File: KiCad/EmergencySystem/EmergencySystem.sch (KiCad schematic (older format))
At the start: 26 parts, among them K1 HE1AN-S-DC12V, K2 HE1AN-S-DC12V, M1 Left_Motor, M2 Right_Motor, SW1 E-StopButton01, SW2 E-StopButton02, SW3 ON/OFF_Switch, SW4 ON/OFF_Switch, SW5 E-Stop_Switch, U1 T3_EmergencyLight_RED, U10 Adafruit_2200mAh_LiPo, U11 OLED_I2C_Display, U2 T3_EmergencyLight_BLUE, U3 T3_EmergencyLight_AMBER, U4 e-Boot_BuckConverter, U5 Elegoo_4RelayModule, U6 Feather_32u4_RFM95, U7 Adafruit_2200mAh_LiPo, U8 Feather_32u4_RFM95, U9 e-Boot_BuckConverter

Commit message: Updated KiCad Schematics
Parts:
- removed SW1: E-StopButton01, symbol Switch:SW_Push_Open
- removed SW2: E-StopButton02, symbol Switch:SW_Push_Open
- removed SW3: ON/OFF_Switch, symbol Switch:SW_SPST
- added SW1: E-Stop_Switch, symbol Switch:SW_SPST
- added SW3: E-StopButton02, symbol Switch:SW_Push_Open
- added SW4: E-StopButton01, symbol Switch:SW_Push_Open
- SW5: value E-Stop_Switch -> ON/OFF_Switch
- renumbered AE2 to AE1, AE1 to AE2, CB2 to CB1, CB1 to CB2, K2 to K1, K1 to K2, M2 to M1, M1 to M2, SW4 to SW2, U8 to U1, U7 to U10, U9 to U11, U1 to U2, U2 to U3, U3 to U4, U10 to U5, U11 to U6, U5 to U7, U4 to U8, U6 to U9
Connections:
- net GND: now also SW2.2 (B), SW1.2 (B), SW3.1 (A)
- net at U9.1 (TXD1/INT3): now also R2.2, SW4.1 (A)
- net at U9.12 (A11): no longer R1.2
- net at U1.1 (TXD1/INT3): now also R1.2, SW1.1 (A)
- new net: SW5.1 (A), U9.~ (EXT_ANT)
- new net: U10.~ (V-), U9.~ (EXT_ANT)
- new net: U1.~ (EXT_ANT), U5.~ (V-)
- new net: SW3.2 (B), SW4.2 (B)
- now unconnected: U1.12 (A11)
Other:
- moved on the sheet: AE1, AE2, SW2, U1, U11, U5, U6

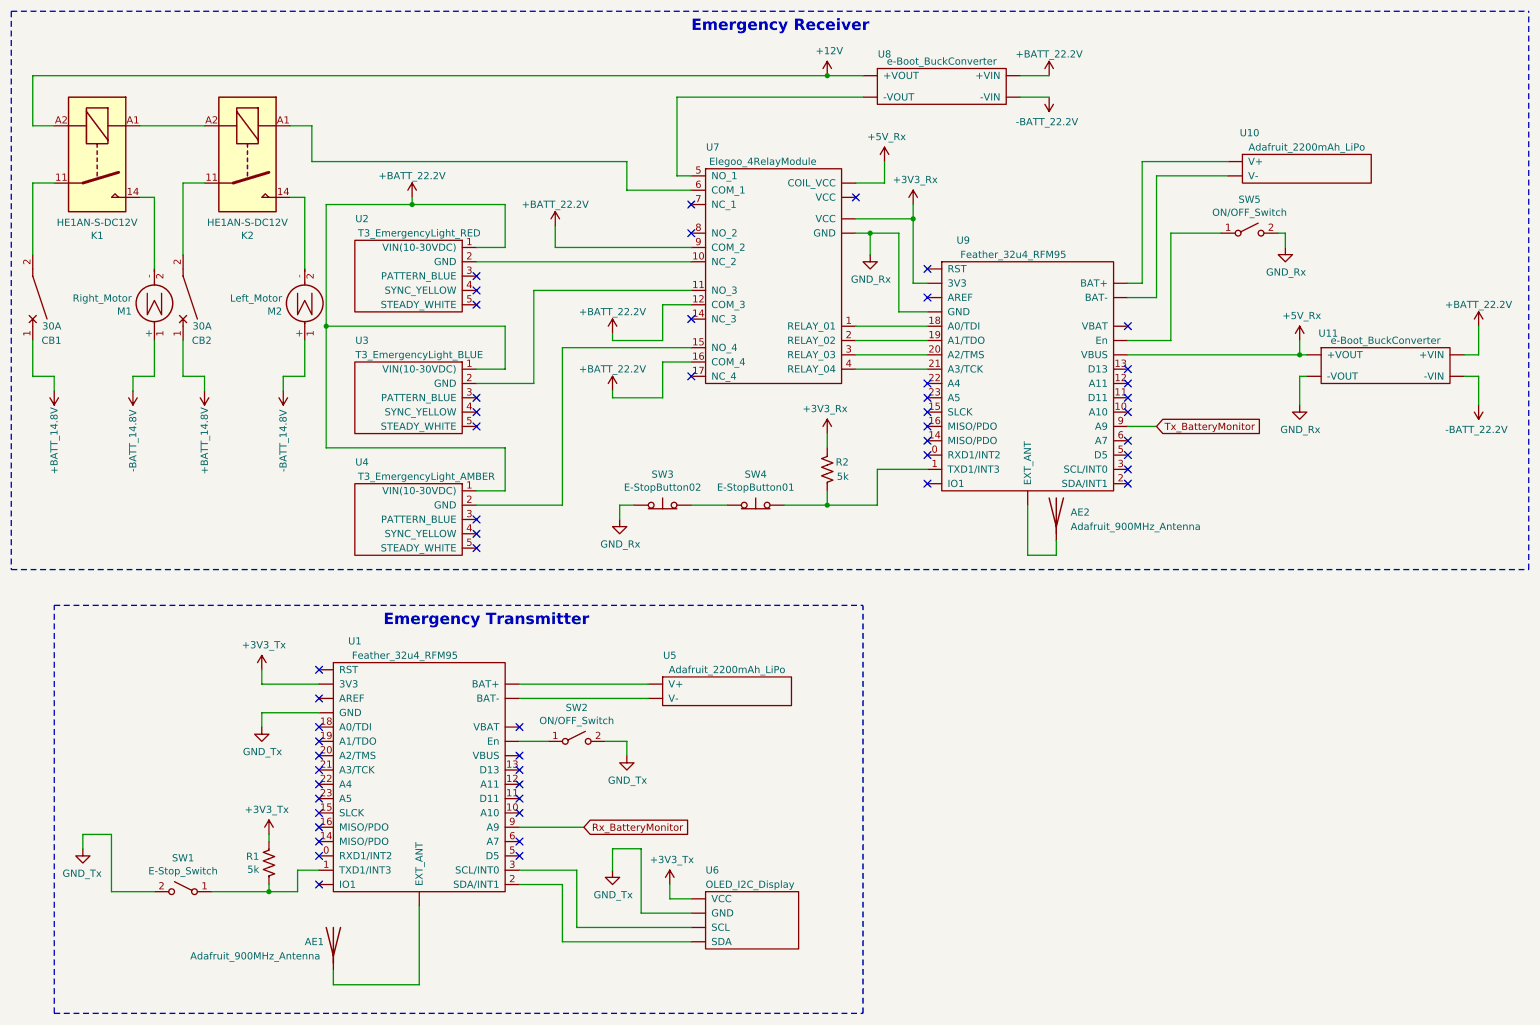
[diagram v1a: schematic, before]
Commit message: updated schematcs and images for presentation
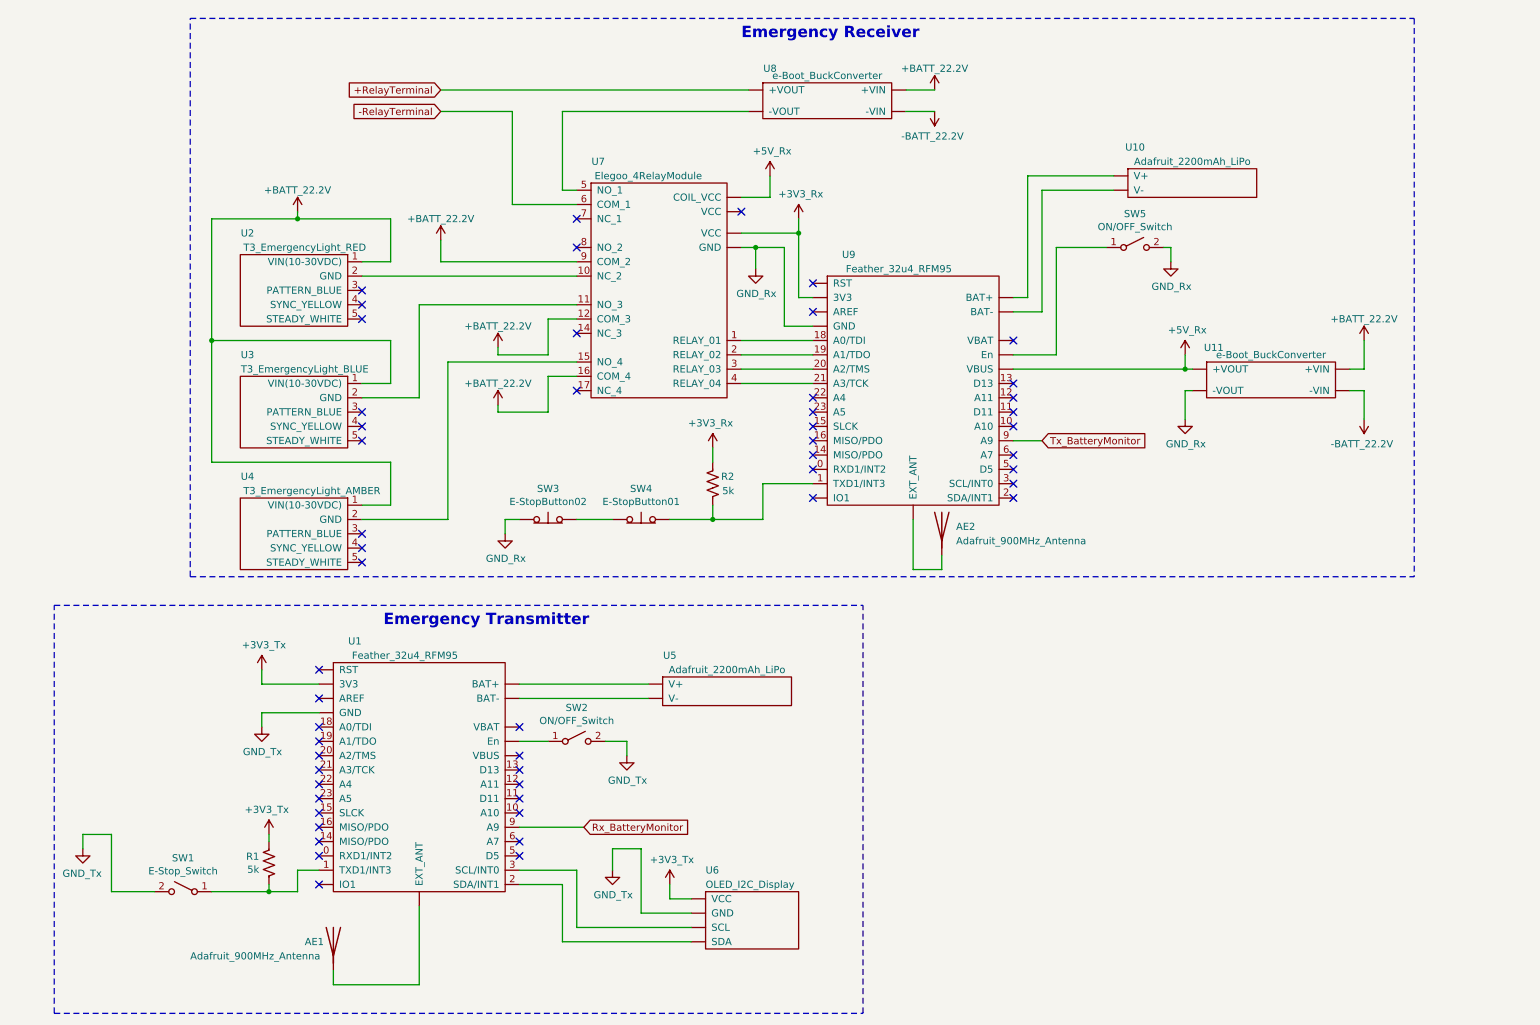
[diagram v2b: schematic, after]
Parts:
- removed CB1, CB2: 30A, symbol Device:CircuitBreaker_1P
- removed K1, K2: HE1AN-S-DC12V, Relay_THT:Relay_SPST_Finder_32.21-x300, symbol Relay:RM50-xx21
- removed M1: Right_Motor, symbol Motor:Motor_DC
- removed M2: Left_Motor, symbol Motor:Motor_DC
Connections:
- net -RelayTerminal: now reaches U7.6 (COM_1)
- net +12V renamed +RelayTerminal
- new net: U10.~ (V-), U9.~ (EXT_ANT)
- new net: U1.~ (EXT_ANT), U5.~ (V-)
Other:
- moved on the sheet: AE2, R2, SW3, SW4, SW5, U10, U11, U2, U3, U4, U7, U8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
